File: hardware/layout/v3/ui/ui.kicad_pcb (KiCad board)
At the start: 4 copper layers, 13.8 x 40.5 mm, 18 parts, among them J1 Carrier, J2 OLED, SW1 PRG/RST, SW2 FUNC, U1 74AHCT1G125

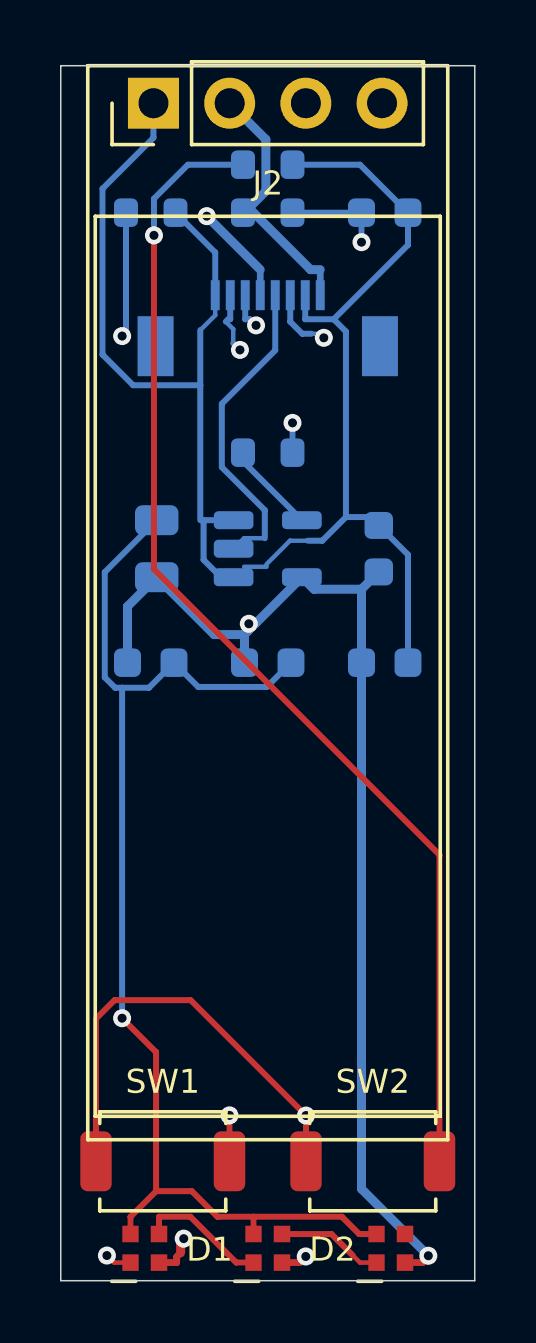
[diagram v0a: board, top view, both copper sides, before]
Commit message: V3 consolidated to two boards (main + ui); updated firmware pin map, button ADC, and OLED connector; removed separate knx/dali boards from CI matrix
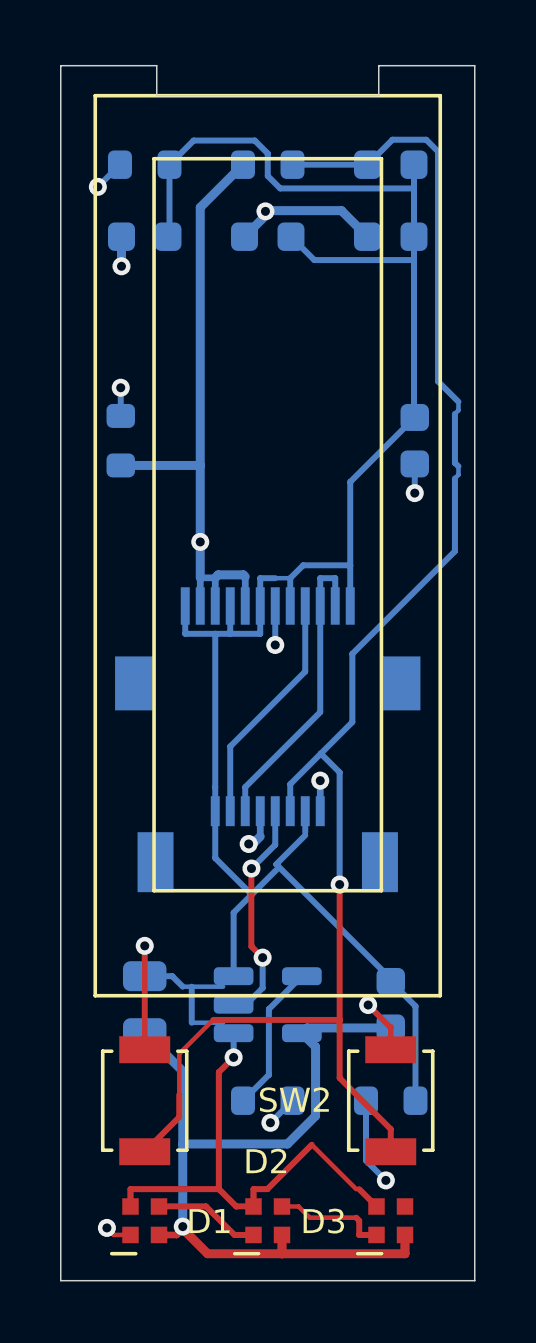
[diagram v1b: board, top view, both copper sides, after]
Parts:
- added C7: 100n 50V, Capacitor_SMD:C_0603_1608Metric, B.Cu at (11.8, -28.0)
- added R5: 10k, Resistor_SMD:R_0603_1608Metric, B.Cu at (2.00, -28.0)
- J2: value OLED -> OLED ZIF; footprint Connector_PinHeader_2.54mm:PinHeader_1x04_P2.54mm_Vertical -> gateway_fp:FPC_XUNPU_FPC-05F-12PH20; moved to B.Cu
- SW1, SW2: footprint Button_Switch_SMD:SW_SPST_TS-1088-xR020 -> Button_Switch_SMD:SW_SPST_B3U-1000P
- moved R3 31.5 mm to (11.0, -6.00)
- moved R4 21.6 mm to (6.90, -6.00)
- moved J2 18.4 mm to (6.90, -21.2), turned to 180 degrees
- moved J1 17.2 mm to (6.90, -14.8)
- moved C2 15.2 mm to (2.80, -9.20)
- moved C3 15.2 mm to (11.0, -9.20)
- moved U1 15.2 mm to (6.90, -9.20)
- moved C4 14.2 mm to (2.80, -34.8)
- moved C6 14.2 mm to (11.0, -34.8)
- moved C5 14.2 mm to (6.90, -34.8)
- moved SW1 2.11 mm to (2.80, -6.00), turned to 90 degrees
- moved SW2 2.11 mm to (11.0, -6.00), turned to 90 degrees
- moved C1 1.61 mm to (11.0, -37.2)
- moved R2 1.61 mm to (2.80, -37.2)
- moved R1 1.60 mm to (6.90, -37.2)
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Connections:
- J2 pad 2: +3V3 -> I2C_SDA
- J2 pad 3: I2C_SCL -> I2C_SDA
- J2 pad 4: I2C_SDA -> I2C_SCL
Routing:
- net N$2: track 39.5 -> 10.8 mm, vias 1 -> 2
- net +3V3: track 8.57 -> 32.1 mm, vias 0 -> 2
- net N$4: track 32.4 -> 10.1 mm
- net OLED_RES: track 0.00 -> 21.7 mm, vias 0 -> 3
- net +5V: track 66.6 -> 76.7 mm, vias 5 -> 4
- net GND: track 95.2 -> 88.7 mm
- net I2C_SCL: track 11.3 -> 7.88 mm, vias 1 -> 0
- net BTN_LADDER: track 50.6 -> 53.8 mm, vias 3 -> 1
- net LED_DATA: track 10.6 -> 7.57 mm, vias 0 -> 2
- net N$1: track 33.2 -> 31.0 mm
- net N$3: track 3.06 -> 4.96 mm
- net LED_CHAIN1: track 4.36 -> 3.54 mm
- net I2C_SDA: track 10.4 -> 10.2 mm, vias 1 -> 0
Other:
- outline, holes or cut-outs redrawn
